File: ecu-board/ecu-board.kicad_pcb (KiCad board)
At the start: 2 copper layers, 180 x 130 mm, 65 parts, among them J1 MicroSquirt_connector, J10 Speed sensor connector, J11 Serial DB9 connector, J12 Cockpit connector, J13 CAN connector, J14 IAT connector, J15 CLT connector, J16 EGO connector, J17 12V connector, J18 PWRGND connector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

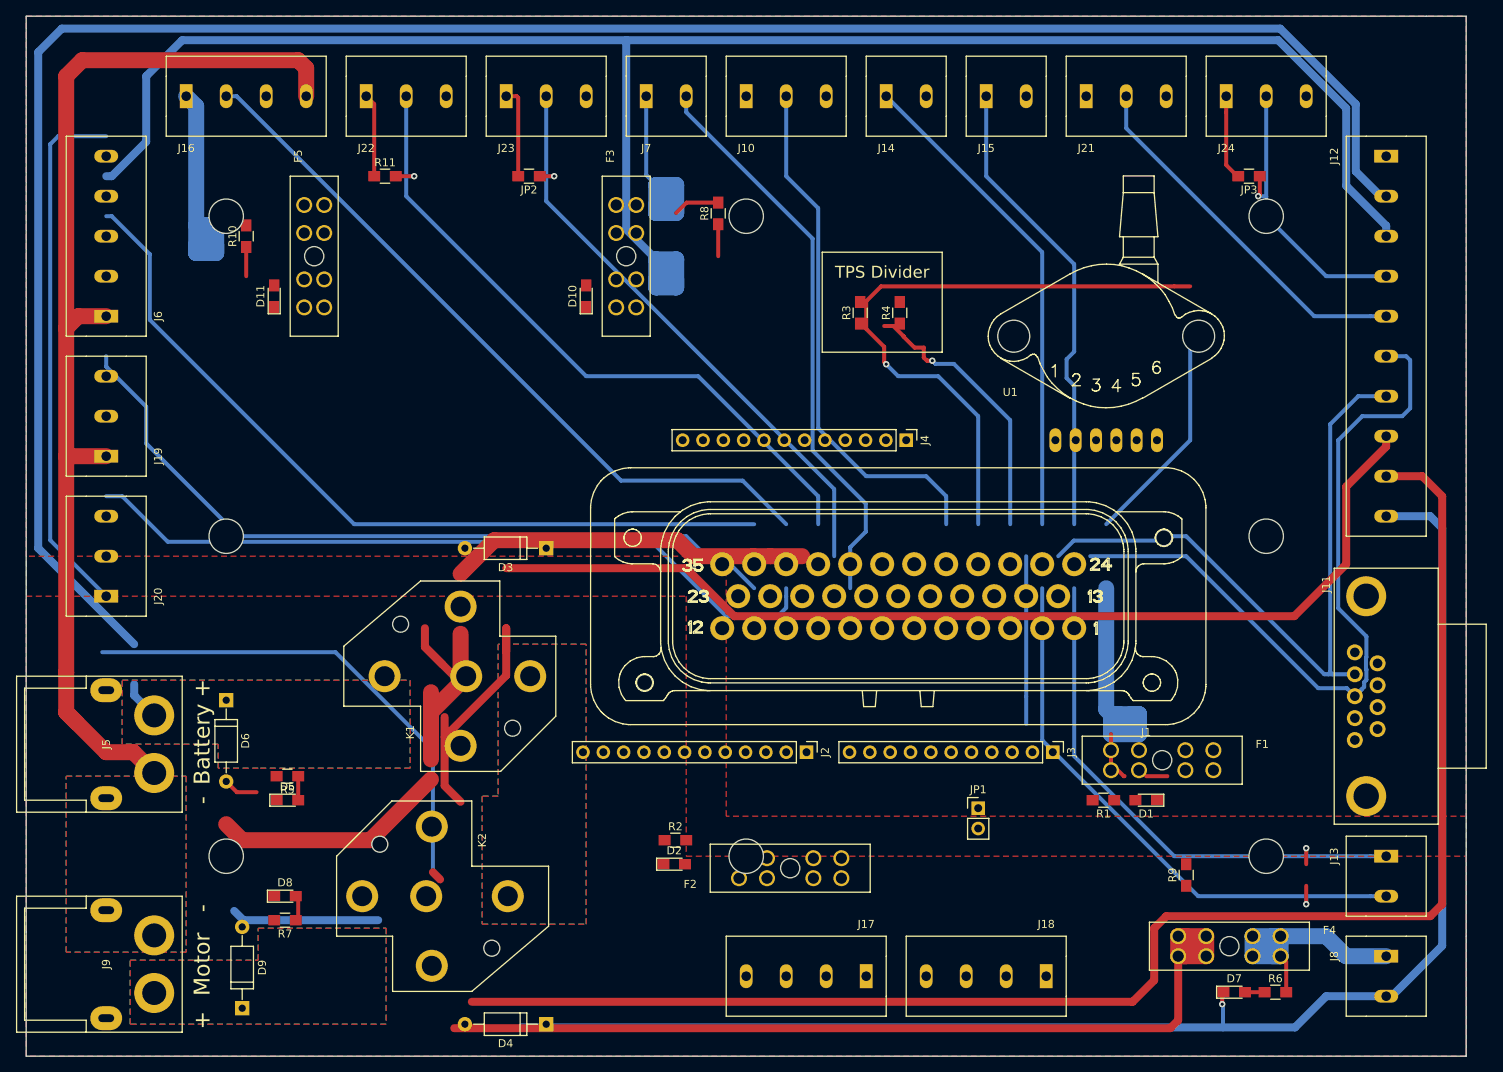
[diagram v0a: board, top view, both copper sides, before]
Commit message: Add connector pinout to silkscreen.
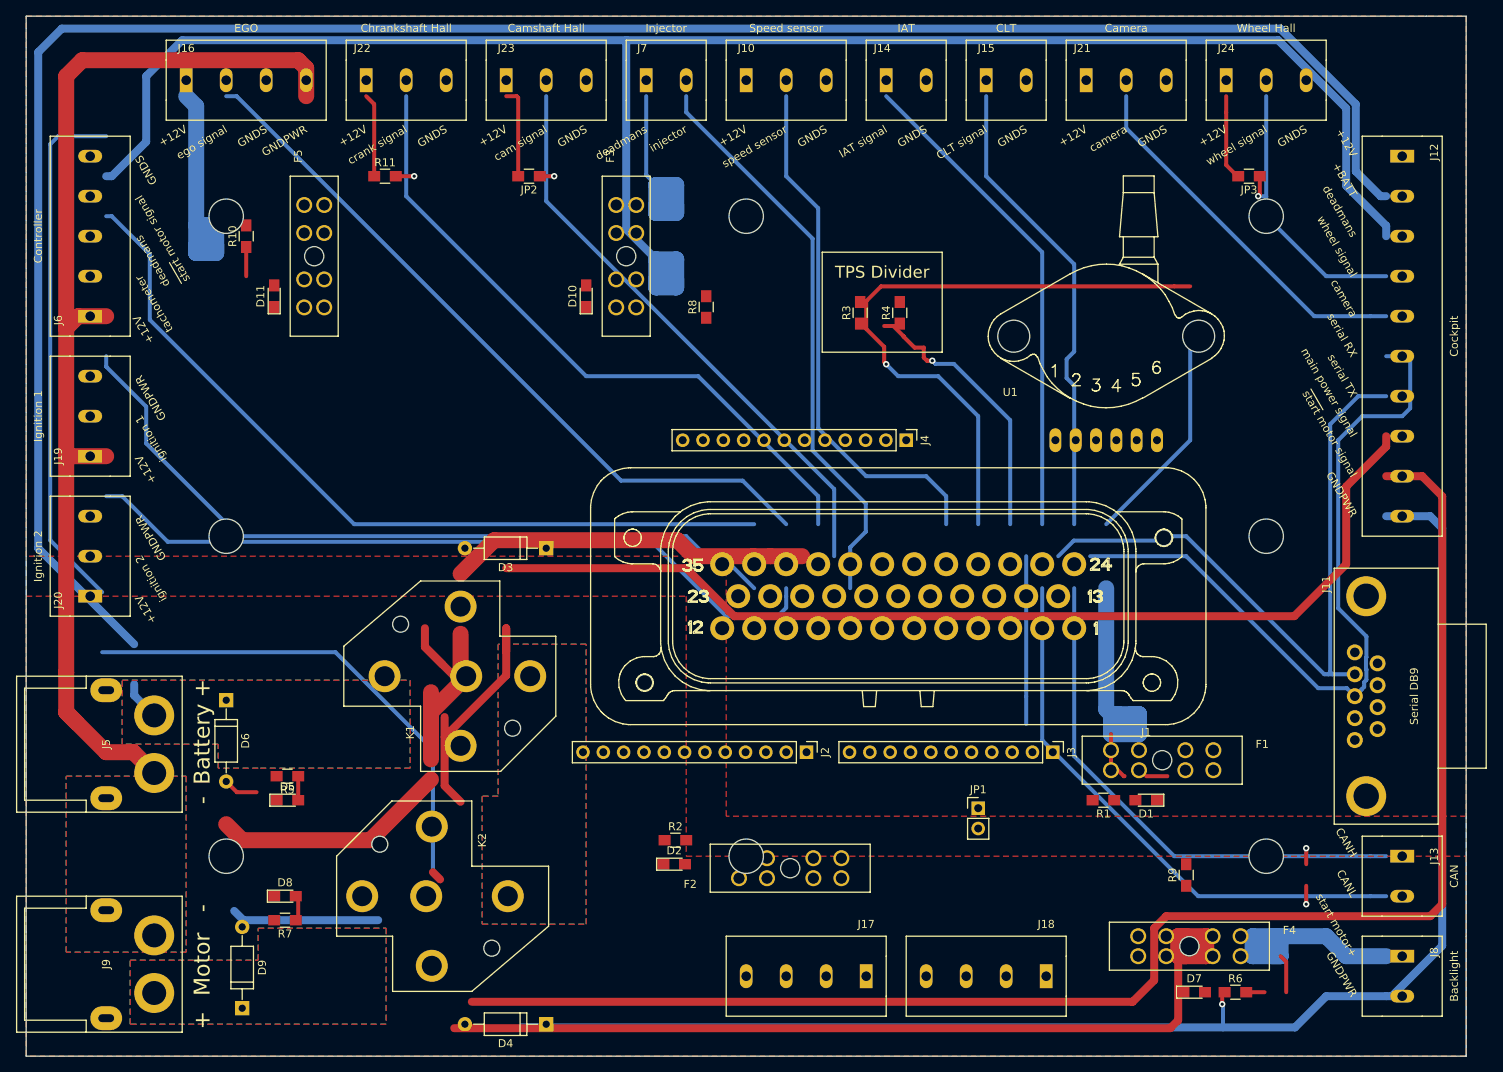
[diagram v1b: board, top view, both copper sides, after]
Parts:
- J10: value Speed sensor connector -> Speed sensor
- J11: value Serial DB9 connector -> Serial DB9
- J12: value Cockpit connector -> Cockpit
- J13: value CAN connector -> CAN
- J14: value IAT connector -> IAT
- J15: value CLT connector -> CLT
- J16: value EGO connector -> EGO
- J19: value Ignition 1 connector -> Ignition 1
- J20: value Ignition 2 connector -> Ignition 2
- J21: value Camera connector -> Camera
- J22: value Chrankshaft Hall connector -> Chrankshaft Hall
- J23: value Camshaft Hall connector -> Camshaft Hall
- J24: value Wheel Hall connector -> Wheel Hall
- J6: value Controller connector -> Controller
- J7: value Injector connector -> Injector
- J8: value Backlight connector -> Backlight
- moved R8 11.8 mm to (120.0, 71.3)
- moved D7 5.00 mm to (181.0, 157.0)
- moved F4 5.00 mm to (180.4, 151.2)
- moved R6 5.00 mm to (186.2, 157.0)
- moved J10 2.00 mm to (125.0, 43.0)
- moved J12 2.00 mm to (207.0, 52.5)
- moved J13 2.00 mm to (207.0, 140.0)
- moved J14 2.00 mm to (142.5, 43.0)
- moved J15 2.00 mm to (155.0, 43.0)
- moved J16 2.00 mm to (55.0, 43.0)
- moved J19 2.00 mm to (43.0, 90.0)
- moved J20 2.00 mm to (43.0, 107.5)
- moved J21 2.00 mm to (167.5, 43.0)
- moved J22 2.00 mm to (77.5, 43.0)
- moved J23 2.00 mm to (95.0, 43.0)
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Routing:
- net +BATT: track 267.2 -> 4.94 mm
- net +12V: track 192.7 -> 455.0 mm
- net /opto_in-: track 0.00 -> 71.6 mm
- net /injector_1: track 71.6 -> 0.00 mm
- net Net-(F1-Pad1): track 45.7 -> 113.9 mm, vias 0 -> 1
- net /CANH: track 68.2 -> 0.00 mm, vias 1 -> 0
- net /clt_signal: track 58.8 -> 0.00 mm
- net GNDS: track 34.4 -> 93.2 mm
- net Net-(F3-Pad2): track 38.5 -> 32.7 mm
- net Net-(D10-Pad2): track 4.00 -> 0.00 mm
- net Net-(F4-Pad2): track 40.1 -> 42.5 mm
- net Net-(D7-Pad2): track 2.45 -> 0.00 mm

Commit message: Add lots of silk screen.
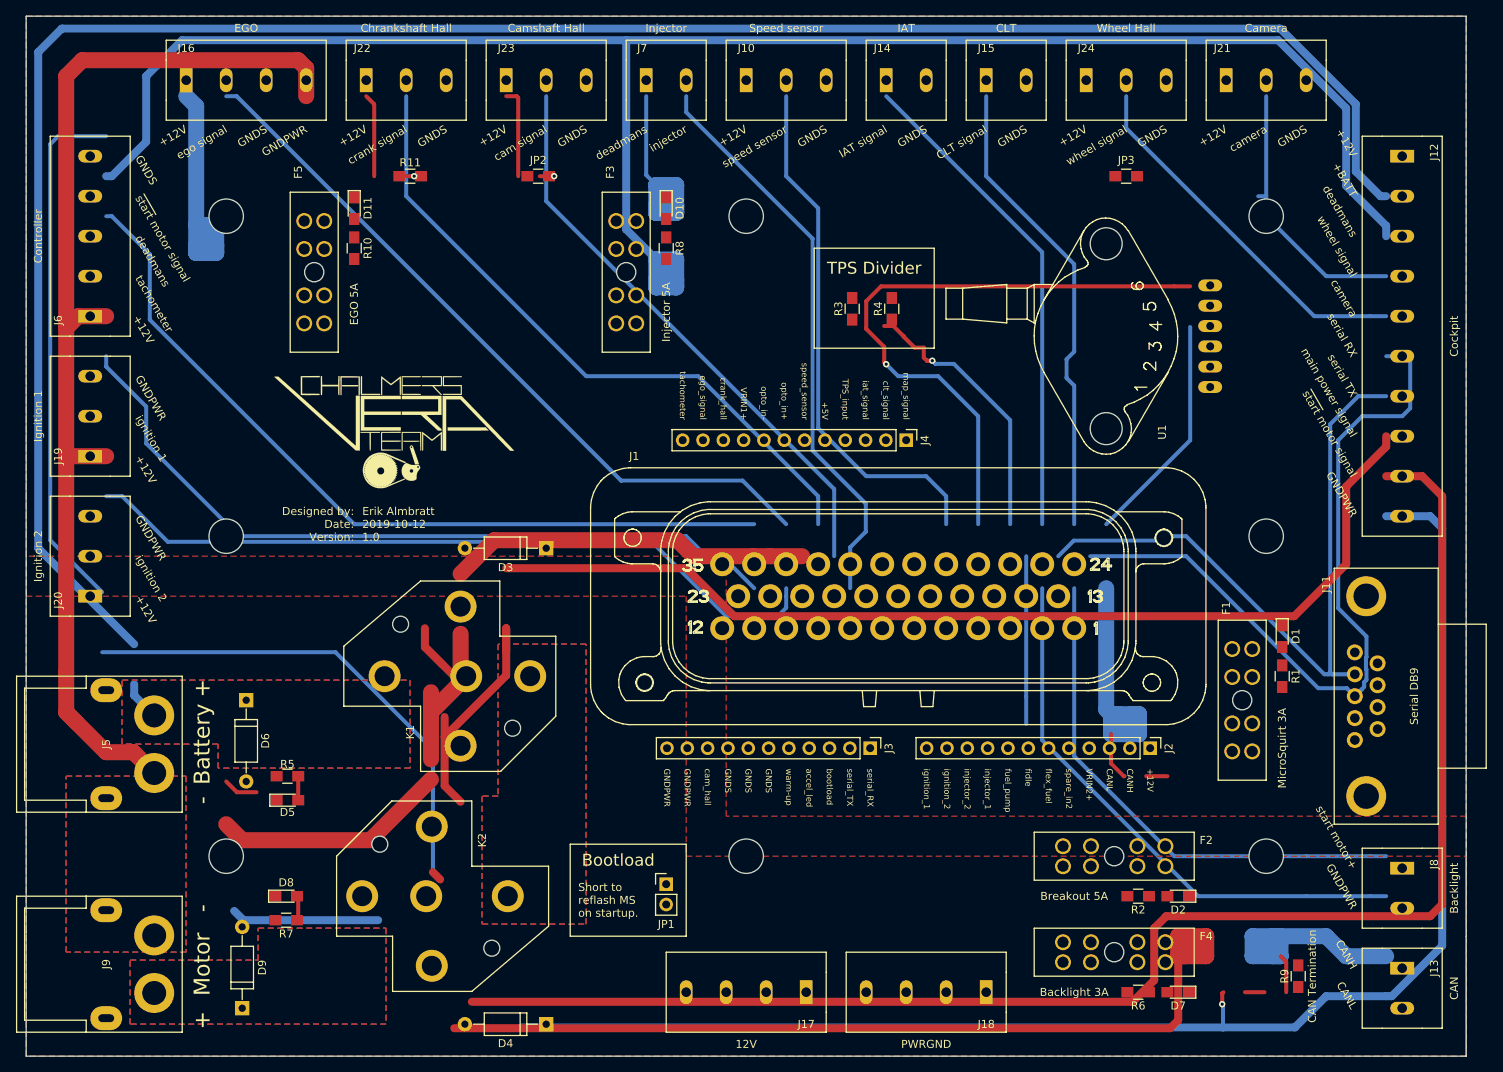
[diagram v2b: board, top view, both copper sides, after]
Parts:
- added G***: LOGO, ecu-board-footprints:Vera-Logo, F.Cu at (81.0, 87.0)
- F1: value 3A Fuse -> MicroSquirt 3A
- F2: value 5A Fuse -> Breakout 5A
- F3: value 5A Fuse -> Injector 5A
- F4: value 3A Fuse -> Backlight 3A
- F5: value 5A Fuse -> EGO 5A
- J17: value 12V connector -> 12V
- J18: value PWRGND connector -> PWRGND
- R9: value 120R -> CAN Termination
- moved D2 63.1 mm to (179.0, 145.0), turned to 180 degrees
- moved R2 58.3 mm to (174.0, 145.0), turned to 180 degrees
- moved J2 43.0 mm to (175.5, 126.5)
- moved F2 40.5 mm to (171.0, 140.0)
- moved JP1 40.1 mm to (115.0, 143.5)
- moved R1 27.2 mm to (192.0, 117.5), turned to 270 degrees
- moved D1 26.6 mm to (192.0, 112.5), turned to 270 degrees
- moved J3 22.8 mm to (140.5, 126.5)
- moved R9 18.9 mm to (194.0, 155.0)
- moved J21 17.5 mm to (185.0, 43.0)
- moved J24 17.5 mm to (167.5, 43.0)
- moved JP3 15.3 mm to (172.5, 55.0)
- moved D10 14.9 mm to (115.0, 59.0), turned to 270 degrees
- moved D11 14.9 mm to (76.0, 59.0), turned to 270 degrees
- moved J13 14.0 mm to (207.0, 154.0)
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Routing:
- net GNDS: track 93.2 -> 221.5 mm
- net /button_to_main_relay: track 128.2 -> 0.00 mm
- net /CANH: track 0.00 -> 70.1 mm
- net /CANL: track 73.4 -> 6.01 mm, vias 1 -> 0
- net +12V: track 455.0 -> 444.3 mm
- net Net-(F1-Pad1): track 113.9 -> 104.9 mm, vias 1 -> 0
- net Net-(F5-Pad2): track 41.5 -> 37.7 mm
- net Net-(D11-Pad2): track 3.65 -> 0.00 mm
- net /Connectors/wheel_signal: track 36.7 -> 34.1 mm, vias 1 -> 0
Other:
- board text added: "Bootload"
- board text added: "Designed by: Date: Version:"
- board text added: "Erik Almbratt 2019-10-12 1.0"
- board text added: "Short to reflash MS on startup."

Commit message: Route full board.
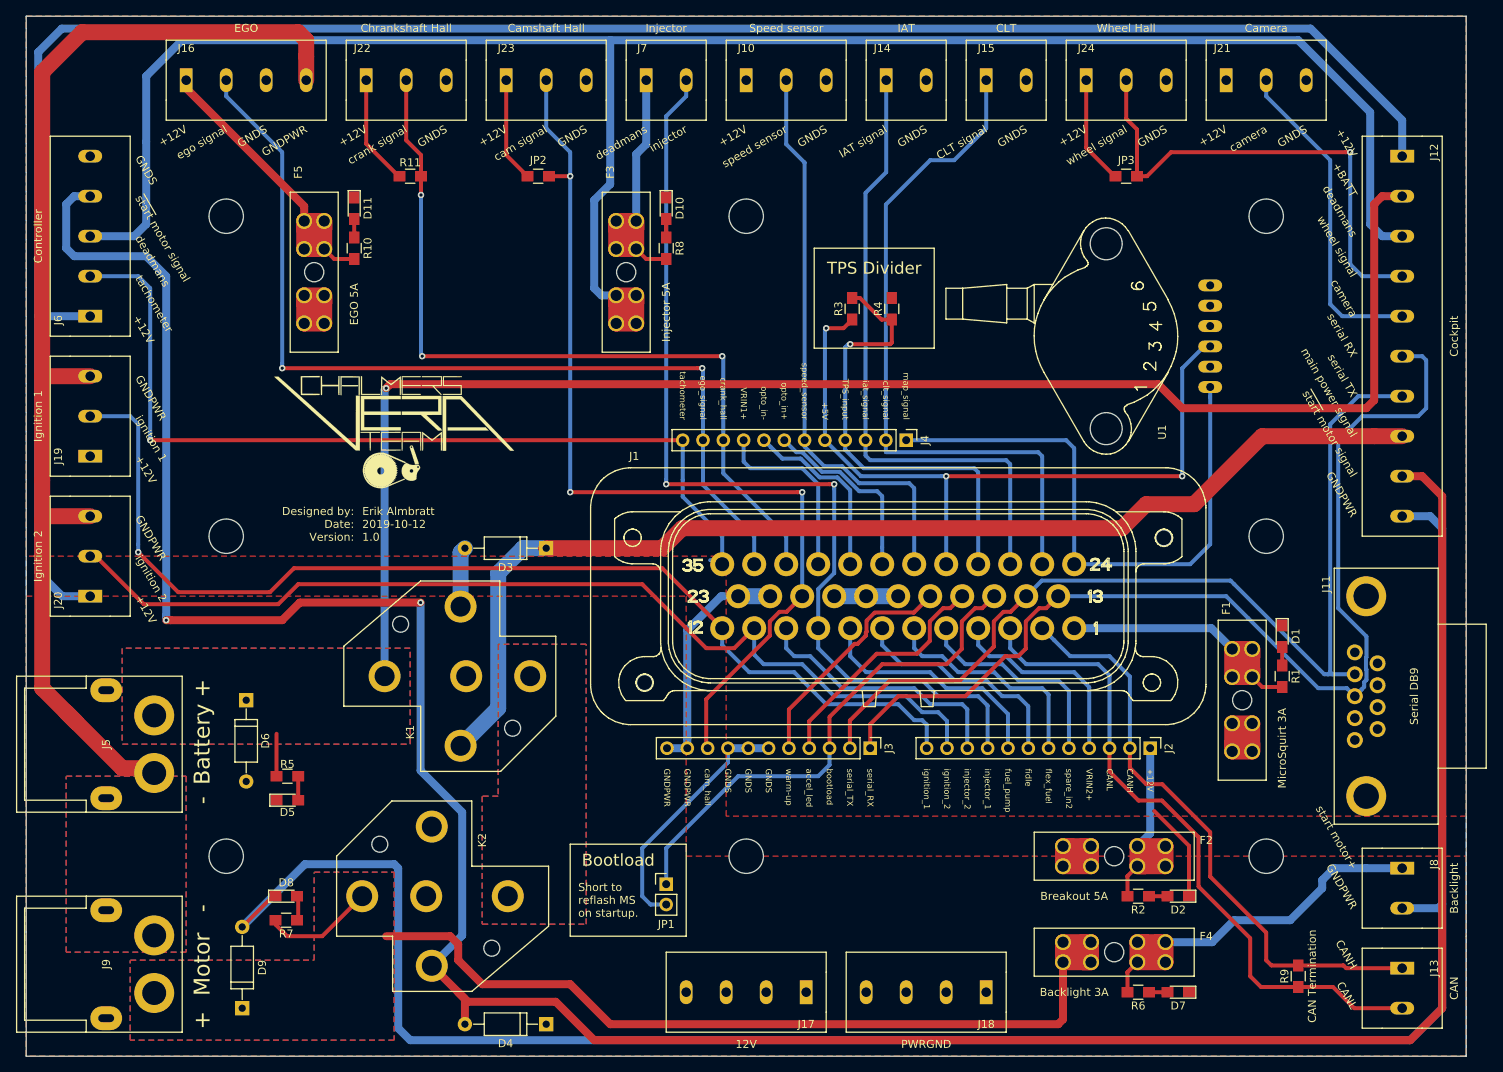
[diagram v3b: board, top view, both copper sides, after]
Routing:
- net +BATT: track 4.94 -> 195.2 mm, vias 0 -> 1
- net GNDS: track 221.5 -> 51.9 mm, vias 1 -> 0
- net /button_to_start_motor_relay: track 189.2 -> 353.9 mm, vias 0 -> 2
- net /button_to_main_relay: track 0.00 -> 143.6 mm
- net /injector_1: track 0.00 -> 123.3 mm, vias 0 -> 2
- net /clt_signal: track 0.00 -> 86.7 mm
- net +12V: track 444.3 -> 363.9 mm
- net /CANL: track 6.01 -> 83.6 mm
- net /bootload: track 0.00 -> 64.1 mm
- net Net-(F1-Pad1): track 104.9 -> 46.2 mm
- net /TPS_input: track 0.00 -> 57.1 mm, vias 0 -> 1
- net /opto_in-: track 71.6 -> 22.6 mm
- net /cam_hall_signal: track 75.2 -> 122.0 mm, vias 1 -> 3
- net /map_signal: track 29.0 -> 73.6 mm
- net /ignition_1: track 96.5 -> 136.6 mm, vias 0 -> 1
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
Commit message: Clean up copper pours.
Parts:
- moved R9 0.50 mm to (194.0, 155.5)
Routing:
- net /injector_1: track 123.3 -> 134.3 mm
- net +BATT: track 195.2 -> 191.9 mm
- net /clt_signal: track 86.7 -> 89.0 mm
- net GNDPWR: track 439.1 -> 440.6 mm
- net /button_to_start_motor_relay: track 353.9 -> 355.4 mm
